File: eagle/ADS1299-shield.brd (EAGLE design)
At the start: 101.6 x 53.3 mm, 133 parts, among them IC1 ADS1299IPAG, IC2 TPS72325DBVT, IC3 TPS73225DBVT, IC5 24AA256UID, IC6 TPS604XXDBV, IC7 OPA376DBV, IC8 OPA376DBV, IC9 TXS0102DCTR, J8 Electrode Connector, U2 TXB0108PWR, U3 TXB0108PWR

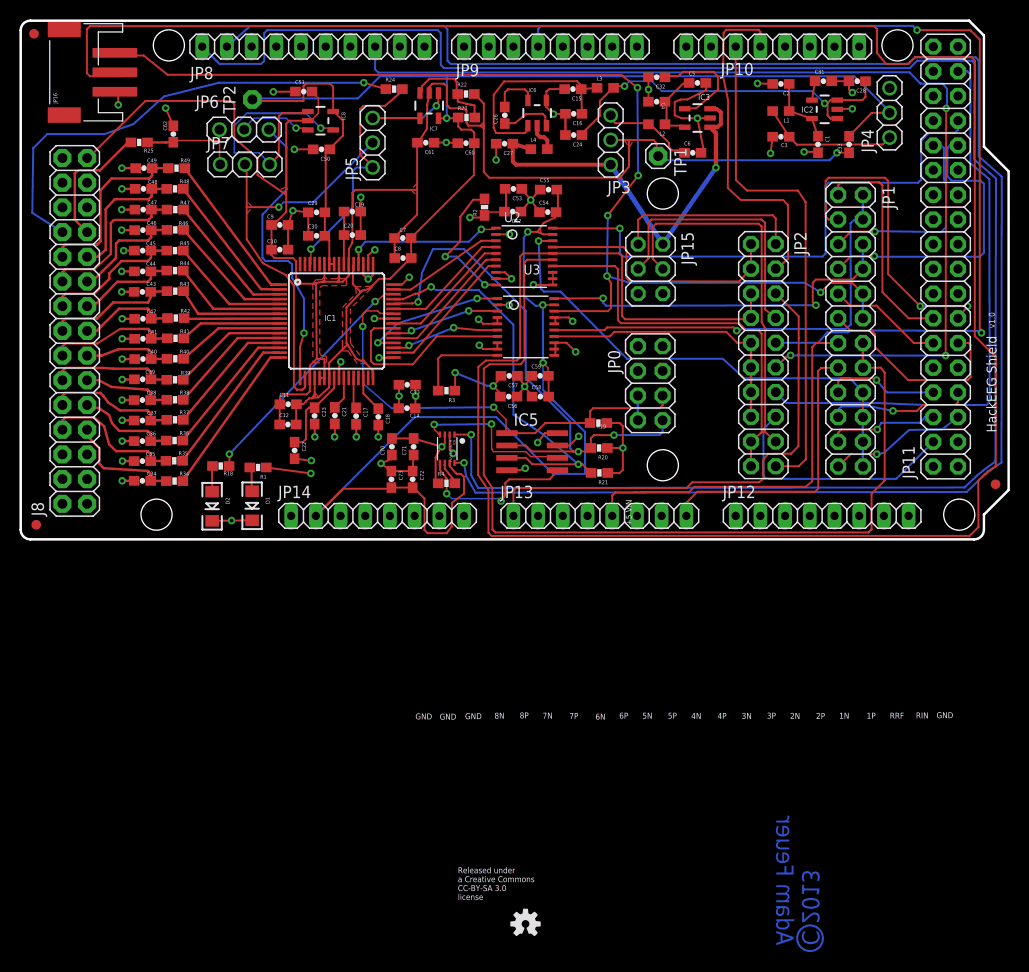
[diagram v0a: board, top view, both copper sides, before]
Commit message: updated headers in SmartPrj to have smaller pads; moved traces away from edge of board; minor clearance improvements; documentation labels for configuration jumpers partly done
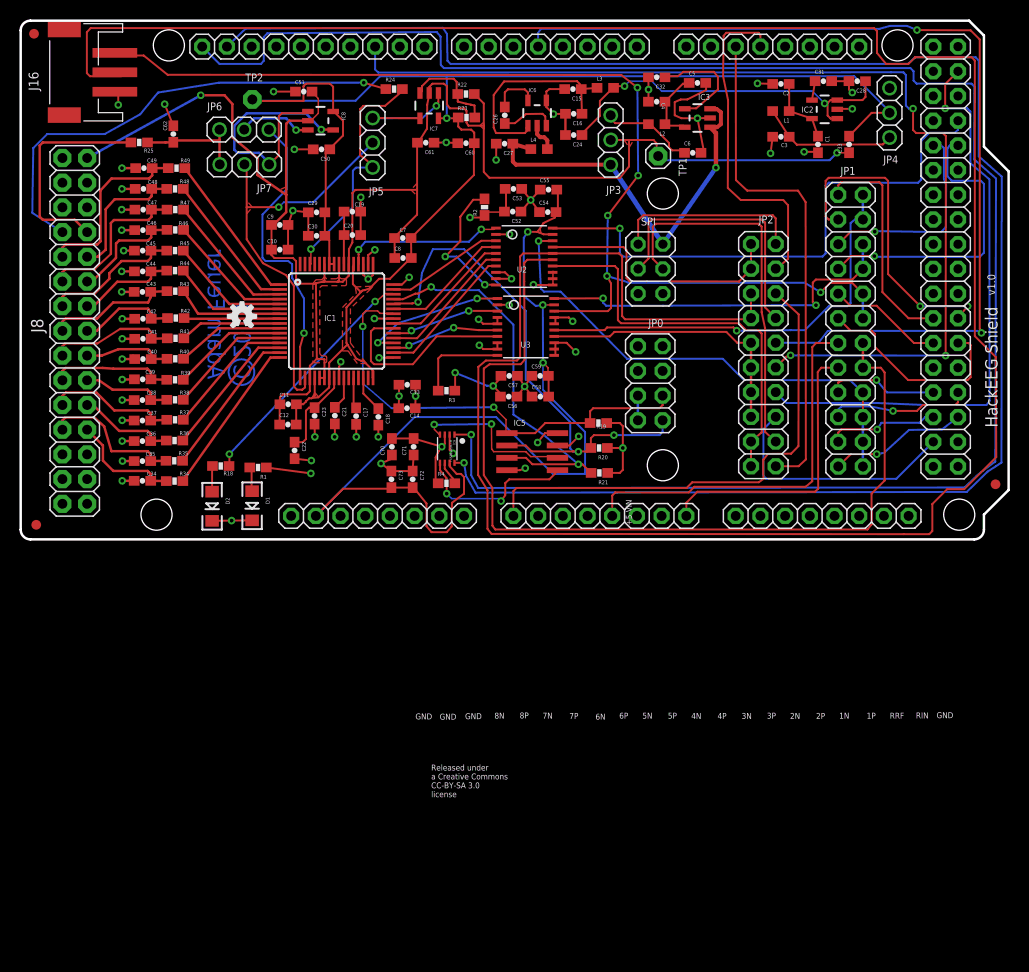
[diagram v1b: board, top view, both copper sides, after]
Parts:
- moved U$1 69.0 mm to (22.9, 23.1)
- moved JP7 0.05 mm to (23.1, 38.7)
- renumbered JP15 to SPI, JP16 to J16
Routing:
- net REF_ELEC_CON: track 13.7 -> 22.7 mm
- net ADS_SPI_CLK: track 269.9 -> 267.5 mm
- net SCL1: track 190.8 -> 188.6 mm
- net !ADC_CS_2: track 58.6 -> 60.4 mm, vias 0 -> 1
- net !ADS_PWDN: track 45.3 -> 44.1 mm
- net ADS_CLK: track 95.3 -> 94.6 mm
- net AGND: track 508.4 -> 509.1 mm
- net USART1_MISO: track 35.9 -> 35.3 mm
- net IOREF: track 103.0 -> 102.5 mm
- net AVDD: track 182.4 -> 182.0 mm, vias 1 -> 2
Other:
- board text added: "0"
- board text added: "1"
- board text added: "10"
- board text added: "11"
- board text added: "12"
- board text added: "2"
- board text added: "3"
- board text added: "31"
- board text added: "32"
- board text added: "4"
- board text added: "5"
- board text added: "6"
- board text added: "7"
- board text added: "8"
- board text added: "9"
- board text added: "Board Addr"
- board text added: "CLK"
- board text added: "DRDY"
- board text added: "Jumper Storage"
- board text added: "PWDN"
- board text added: "RESET"
- board text added: "SPI CLK"
- board text added: "SPI CS"
- board text added: "SPI MISO"
- board text added: "SPI MOSI"
- board text added: "START"

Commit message: documentation labels done; OSH and CC logos on back of board; increased size of component names for better readability
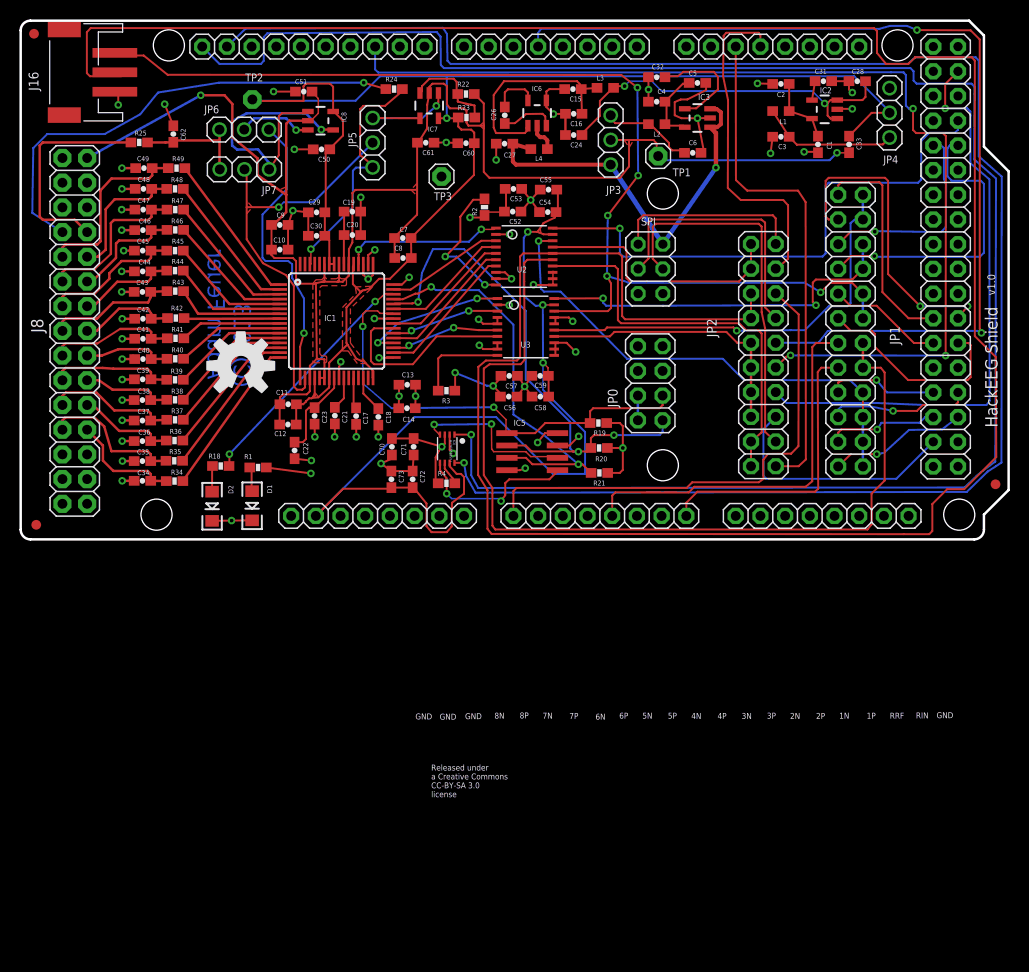
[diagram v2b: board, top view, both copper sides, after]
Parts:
- added TP3: AGND_TEST_POINT, adafruit:1X01
- added U$3: (no value), creative-commons:CC-BY-SA
- added U$4: (no value), SparkFun-Aesthetics:OSHW-LOGO-L
- U$1: device SparkFun-Aesthetics:OSHW-LOGO-S -> SparkFun-Aesthetics:OSHW-LOGO-L
- moved U$1 5.08 mm to (22.8, 18.0)
- moved JP7 0.51 mm to (23.1, 38.2)
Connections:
- net AGND: now also TP3.1
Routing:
- net AGND: track 509.1 -> 514.9 mm
- net N$17: track 26.8 -> 28.2 mm
- net REF_ELEC: track 11.1 -> 11.6 mm
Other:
- board text added: "A"
- board text added: "B"
- board text removed: "+5 VIN"

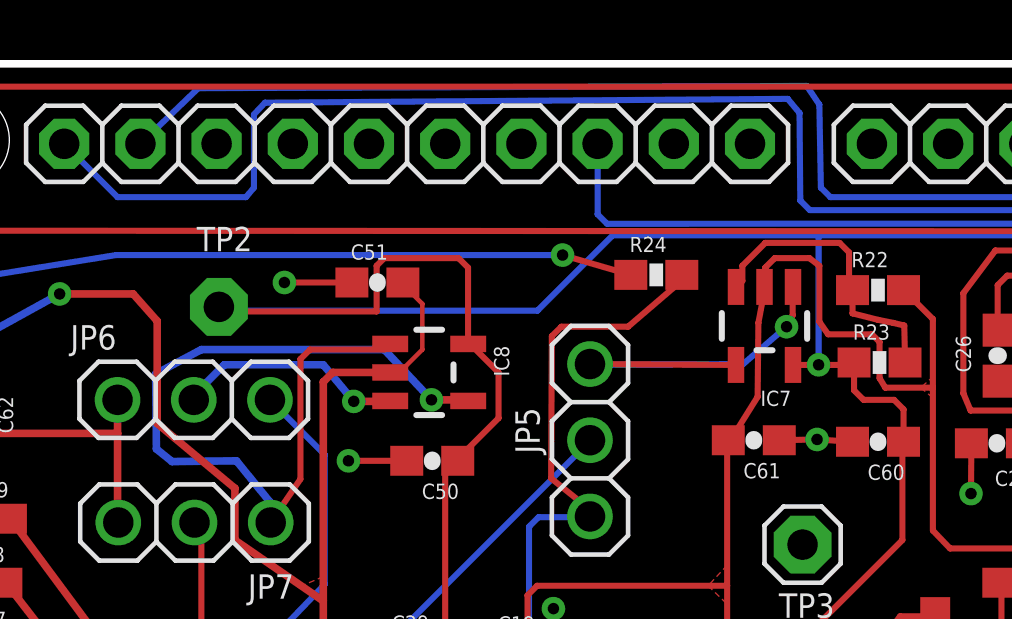
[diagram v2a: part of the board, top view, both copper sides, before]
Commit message: fixed problem with test point 2
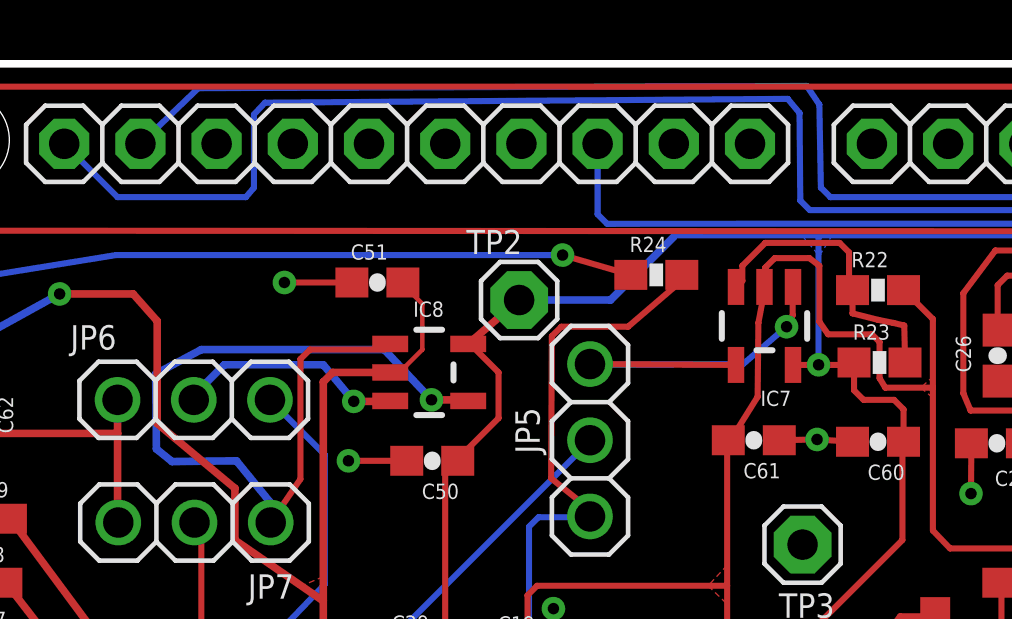
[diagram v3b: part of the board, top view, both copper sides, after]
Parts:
- moved TP2 10.0 mm to (34.0, 45.6), flipped to the top, turned to 0 degrees
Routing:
- net AVSS: track 162.5 -> 141.9 mm
- net AGND: track 514.9 -> 514.3 mm
- added copper zone on layer 16, net AVSS
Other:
- board text added: "C"
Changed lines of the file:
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@@
 <grid distance="4" unitdist="mil" unit="mil" style="lines" multiple="1" display="yes" altdistance="0.001" altunitdist="inch" altunit="inch"/>
 <layers>
-<layer number="1" name="Top" color="4" fill="1" visible="yes" active="yes"/>
-<layer number="2" name="AGND" color="3" fill="1" visible="yes" active="yes"/>
+<layer number="1" name="Top" color="4" fill="1" visible="no" active="yes"/>
+<layer number="2" name="AGND" color="3" fill="1" visible="no" active="yes"/>
 <layer number="3" name="Route3" color="4" fill="3" visible="no" active="no"/>
 <layer number="14" name="Route14" color="1" fill="6" visible="no" active="no"/>
-<layer number="15" name="DVDD" color="15" fill="1" visible="yes" active="yes"/>
+<layer number="15" name="DVDD" color="15" fill="1" visible="no" active="yes"/>
 <layer number="16" name="Bottom" color="1" fill="1" visible="yes" active="yes"/>
 <layer number="17" name="Pads" color="2" fill="1" visible="yes" active="yes"/>
@@
 <text x="9.5758" y="38.608" size="0.8128" layer="51" rot="R90">32</text>
 <text x="9.8044" y="3.3274" size="0.8128" layer="51" rot="R90">2</text>
-<text x="38.7858" y="38.0238" size="0.8128" layer="51" rot="R90">1</text>
-<text x="38.7858" y="40.5638" size="0.8128" layer="51" rot="R90">2</text>
-<text x="38.7858" y="43.1038" size="0.8128" layer="51" rot="R90">3</text>
-<text x="63.2714" y="38.354" size="0.8128" layer="51" rot="R90">1</text>
-<text x="63.1952" y="40.9956" size="0.8128" layer="51" rot="R90">2</text>
-<text x="63.1698" y="43.5356" size="0.8128" layer="51" rot="R90">3</text>
+<text x="38.7858" y="38.0238" size="0.8128" layer="51" rot="R90">A</text>
+<text x="38.7858" y="40.5638" size="0.8128" layer="51" rot="R90">B</text>
+<text x="38.7858" y="43.1038" size="0.8128" layer="51" rot="R90">C</text>
+<text x="63.2714" y="38.354" size="0.8128" layer="51" rot="R90">A</text>
+<text x="63.1952" y="40.9956" size="0.8128" layer="51" rot="R90">B</text>
+<text x="63.1698" y="43.5356" size="0.8128" layer="51" rot="R90">C</text>
 <text x="75.565" y="32.8676" size="0.8128" layer="51" rot="R90">A</text>
 <text x="78.232" y="32.893" size="0.8128" layer="51" rot="R90">B</text>
 <text x="84.3026" y="37.7444" size="0.8128" layer="51" rot="R90">A</text>
 <text x="87.376" y="37.7698" size="0.8128" layer="51" rot="R90">B</text>
-<text x="20.8026" y="40.5638" size="0.8128" layer="51" rot="R180">1</text>
-<text x="23.5458" y="40.5638" size="0.8128" layer="51" rot="R180">2</text>
-<text x="26.0858" y="40.5638" size="0.8128" layer="51" rot="R180">3</text>
-<text x="91.9226" y="41.1734" size="0.8128" layer="51" rot="R90">1</text>
-<text x="91.821" y="43.7134" size="0.8128" layer="51" rot="R90">2</text>
-<text x="91.9226" y="46.2534" size="0.8128" layer="51" rot="R90">3</text>
+<text x="20.8026" y="40.5638" size="0.8128" layer="51" rot="R180">A</text>
+<text x="23.5458" y="40.5638" size="0.8128" layer="51" rot="R180">B</text>
+<text x="26.0858" y="40.5638" size="0.8128" layer="51" rot="R180">C</text>
+<text x="91.9226" y="41.1734" size="0.8128" layer="51" rot="R90">A</text>
+<text x="91.821" y="43.7134" size="0.8128" layer="51" rot="R90">B</text>
+<text x="91.9226" y="46.2534" size="0.8128" layer="51" rot="R90">C</text>
 <wire x1="67.2592" y1="16.256" x2="68.8848" y2="16.256" width="0.254" layer="51"/>
 <wire x1="68.8848" y1="16.256" x2="68.8848" y2="15.748" width="0.254" layer="51"/>
@@
 </element>
 <element name="IC8" library="OPA376" package="SOT23-5" value="OPA376DBV" x="30.9626" y="43.18" smashed="yes" rot="R270">
-<attribute name="NAME" x="33.1216" y="44.069" size="0.508" layer="25" font="vector" rot="R270"/>
+<attribute name="NAME" x="30.4292" y="45.0342" size="0.508" layer="25" font="vector"/>
 <attribute name="VALUE" x="30.7721" y="44.1325" size="0.4064" layer="27" rot="R270"/>
 </element>
@@
 <attribute name="VALUE" x="68.8594" y="38.2778" size="1.27" layer="27" rot="R90"/>
 </element>
-<element name="TP2" library="adafruit" package="1X01" value="AVSS_TEST_POINT" x="23.9522" y="45.3644" smashed="yes" rot="MR90">
-<attribute name="NAME" x="25.0698" y="48.0314" size="0.8128" layer="25" font="vector" ratio="10" rot="R180"/>
-<attribute name="VALUE" x="20.7772" y="44.0944" size="1.27" layer="27" rot="R90"/>
-</element>
 <element name="U$5" library="adafruit" package="FIDUCIAL_1MM" value="FIDUCIAL" x="1.4986" y="52.1208" smashed="yes"/>
 <element name="U$6" library="adafruit" package="FIDUCIAL_1MM" value="FIDUCIAL" x="100.3808" y="5.7912" smashed="yes"/>
@@
 <element name="U$3" library="creative-commons" package="CC-BY-SA" value="" x="81.8896" y="32.385" rot="MR0"/>
 <element name="U$4" library="SparkFun-Aesthetics" package="OSHW-LOGO-L" value="" x="22.6568" y="25.4" rot="MR0"/>
+<element name="TP2" library="adafruit" package="1X01" value="AVSS_TEST_POINT" x="33.9598" y="45.593" smashed="yes">
+<attribute name="NAME" x="32.2072" y="47.117" size="0.8128" layer="25" ratio="10"/>
+<attribute name="VALUE" x="32.6898" y="42.418" size="1.27" layer="27"/>
+</element>
 </elements>
 <signals>
@@
 <wire x1="64.682" y1="45.1358" x2="64.6938" y2="46.3804" width="0.2032" layer="1"/>
 <contactref element="J16" pad="1"/>
-<wire x1="26.1366" y1="46.1772" x2="25.0698" y2="46.9392" width="0.2032" layer="2"/>
-<wire x1="25.0698" y1="46.9392" x2="22.3012" y2="46.9646" width="0.2032" layer="2"/>
-<wire x1="22.3012" y1="46.9646" x2="20.066" y2="44.7548" width="0.2032" layer="2"/>
-<wire x1="20.066" y1="44.7548" x2="14.9352" y2="44.8818" width="0.2032" layer="2"/>
 <wire x1="9.812" y1="46.1584" x2="9.8425" y2="46.1584" width="0.2032" layer="1"/>
 <wire x1="9.8425" y1="46.1584" x2="10.16" y2="45.8409" width="0.2032" layer="1"/>
@@
 <wire x1="43.4086" y1="37.465" x2="43.3832" y2="37.4904" width="0.254" layer="2"/>
 <wire x1="43.3832" y1="37.4904" x2="49.022" y2="39.1414" width="0.254" layer="2"/>
+<wire x1="14.9352" y1="44.8818" x2="24.8412" y2="44.8818" width="0.254" layer="2"/>
+<wire x1="24.8412" y1="44.8818" x2="26.1366" y2="46.1772" width="0.254" layer="2"/>
 <wire x1="70.4088" y1="39.9288" x2="70.0904" y2="39.878" width="0" layer="19" extent="1-1"/>
 <wire x1="51.9176" y1="15.8496" x2="51.95494375" y2="15.853746875" width="0" layer="19" extent="1-2"/>
@@
 <contactref element="C33" pad="2"/>
 <contactref element="JP4" pad="2"/>
-<contactref element="TP2" pad="1"/>
 <contactref element="C11" pad="2"/>
 <contactref element="C12" pad="2"/>
@@
 <wire x1="32.258" y1="28.448" x2="32.3636" y2="28.4306" width="0.1524" layer="1"/>
 <wire x1="32.004" y1="28.448" x2="31.8636" y2="28.4306" width="0.1524" layer="1"/>
-<wire x1="29.21" y1="45.212" x2="24.13" y2="45.212" width="0.2032" layer="1"/>
-<wire x1="29.21" y1="46.736" x2="29.21" y2="45.212" width="0.2032" layer="1"/>
-<wire x1="29.464" y1="46.99" x2="29.21" y2="46.736" width="0.2032" layer="1"/>
-<wire x1="32.258" y1="44.196" x2="32.258" y2="46.6725" width="0.2032" layer="1"/>
-<wire x1="32.258" y1="46.6725" x2="31.9405" y2="46.99" width="0.2032" layer="1"/>
-<wire x1="31.9405" y1="46.99" x2="29.464" y2="46.99" width="0.2032" layer="1"/>
-<wire x1="24.13" y1="45.212" x2="23.9522" y2="45.3644" width="0.254" layer="1"/>
-<wire x1="32.258" y1="44.196" x2="32.2627" y2="44.13" width="0.1524" layer="1"/>
 <wire x1="85.852" y1="47.752" x2="89.408" y2="44.196" width="0.2032" layer="16"/>
-<wire x1="37.084" y1="47.752" x2="43.942" y2="47.752" width="0.2032" layer="16"/>
+<wire x1="39.116" y1="47.752" x2="43.942" y2="47.752" width="0.2032" layer="16"/>
 <wire x1="43.942" y1="47.752" x2="85.852" y2="47.752" width="0.2032" layer="16"/>
-<wire x1="34.5694" y1="45.2374" x2="37.084" y2="47.752" width="0.2032" layer="16"/>
-<wire x1="24.13" y1="45.2374" x2="34.5694" y2="45.2374" width="0.2032" layer="16"/>
 <wire x1="89.408" y1="44.196" x2="89.4842" y2="43.9928" width="0.1524" layer="16"/>
-<wire x1="24.13" y1="45.2374" x2="23.9522" y2="45.3644" width="0.254" layer="16"/>
 <wire x1="43.942" y1="47.752" x2="43.942" y2="43.434" width="0.2032" layer="16"/>
 <wire x1="43.942" y1="43.434" x2="43.942" y2="43.4293" width="0.1524" layer="1"/>
@@
 <wire x1="34.29" y1="28.194" x2="34.29" y2="26.37470625" width="0.2032" layer="1"/>
 <wire x1="34.29" y1="26.37470625" x2="35.112028125" y2="25.552678125" width="0.2032" layer="1"/>
+<contactref element="TP2" pad="1"/>
+<wire x1="33.9598" y1="45.593" x2="32.2627" y2="44.13" width="0.254" layer="1"/>
+<wire x1="39.116" y1="47.752" x2="39.116" y2="47.7012" width="0.2032" layer="16"/>
+<wire x1="39.116" y1="47.7012" x2="37.0078" y2="45.593" width="0.254" layer="16"/>
+<wire x1="37.0078" y1="45.593" x2="33.9598" y2="45.593" width="0.254" layer="16"/>
+<polygon width="0.0254" layer="16">
+<vertex x="43.3832" y="47.752"/>
+<vertex x="43.9674" y="47.0662"/>
+<vertex x="44.3992" y="47.752"/>
+</polygon>
 </signal>
 <signal name="N$561">
